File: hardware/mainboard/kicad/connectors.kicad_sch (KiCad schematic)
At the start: 14 parts, among them J5 GCT USB4105-GF-A-120, J6 4-pin pogo dock, J7 Tag-Connect TC2030-IDC-NL, U8 USBLC6-2SC6

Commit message: R30: align J6 bare contact BOM and J7 service header value with schematic
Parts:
- J6: now left out of the parts list
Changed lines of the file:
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@@
 	(global_label "USB_SHIELD" (shape input) (at 60.96 144.78 0) (effects (font (size 0.9 0.9)) (justify right bottom)))
 	(global_label "GND" (shape output) (at 76.2 144.78 180) (effects (font (size 0.9 0.9)) (justify right bottom)))
-	(symbol (lib_id "ENKU:DOCK4") (at 160.02 68.58 0) (unit 1) (exclude_from_sim no) (in_bom yes) (on_board yes) (dnp no)
+	(symbol (lib_id "ENKU:DOCK4") (at 160.02 68.58 0) (unit 1) (exclude_from_sim no) (in_bom no) (on_board yes) (dnp no)
 		(property "Reference" "J6" (at 150.02 52.58 0) (effects (font (size 0.9 0.9))))
 		(property "Value" "4-pin pogo dock" (at 170.02 52.58 0) (effects (font (size 0.9 0.9))))

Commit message: R41: correct ST ESD lands and route USB CC/VBUS power; fix GND clearances
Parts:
- U8: footprint Package_TO_SOT_SMD:SOT-23-6 -> ENKU:USBLC6_2SC6_ST_SOT23_6L
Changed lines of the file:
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@@
 		(property "Reference" "U8" (at 96.41 58.93 0) (effects (font (size 0.9 0.9))))
 		(property "Value" "USBLC6-2SC6" (at 114.41 58.93 0) (effects (font (size 0.9 0.9))))
-		(property "Footprint" "Package_TO_SOT_SMD:SOT-23-6" (at 105.41 74.93 0) (effects (font (size 0.9 0.9)) (hide yes)))
+		(property "Footprint" "ENKU:USBLC6_2SC6_ST_SOT23_6L" (at 105.41 74.93 0) (effects (font (size 0.9 0.9)) (hide yes)))
 		(property "Datasheet" "~" (at 105.41 74.93 0) (effects (font (size 0.9 0.9)) (hide yes)))
 		(property "Description" "USBLC6-2SC6" (at 105.41 74.93 0) (effects (font (size 0.9 0.9)) (hide yes)))

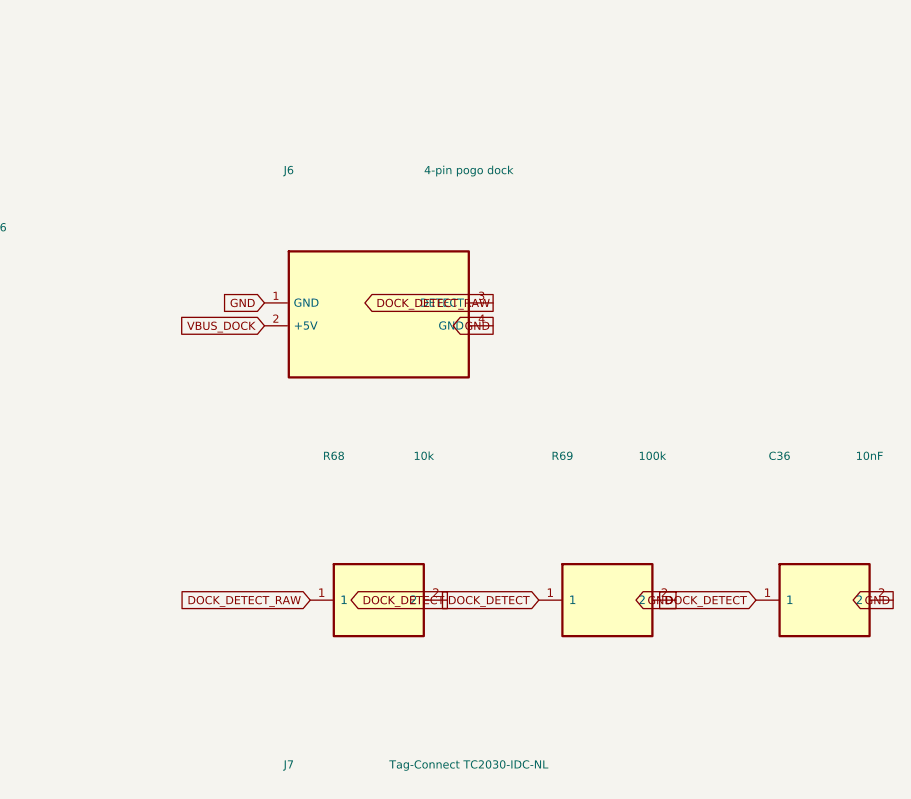
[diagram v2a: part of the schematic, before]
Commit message: hardware: preserve recovered R119 layout and verified R118 source [skip ci]
Persist the KiCad 10.0.7 project before the next routing pass. The recovered layout has 67 opens, ERC 0, parity 0 and zero RF keepout violations; routing is incomplete and fabrication is blocked. Preserve all pad and surviving copper net identities and retain an immutable R118 source archive.
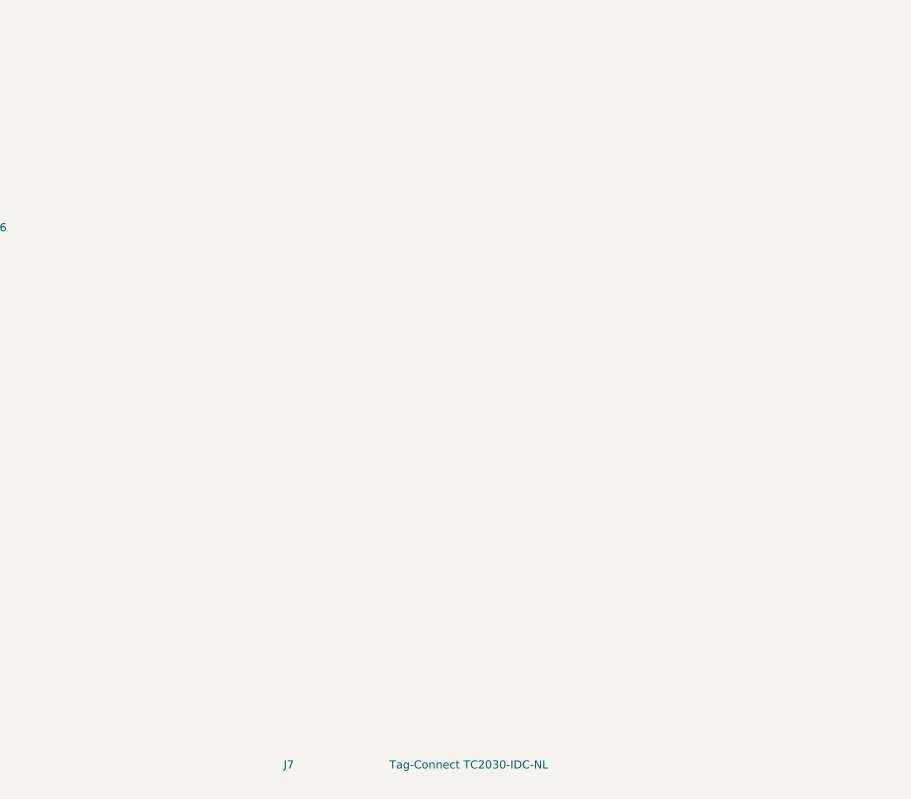
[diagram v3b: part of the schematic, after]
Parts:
- removed C36: 10nF, Capacitor_SMD:C_0603_1608Metric, symbol ENKU:C
- removed J6: 4-pin pogo dock, ENKU:DOCK_POGO_4, symbol ENKU:DOCK4
- removed R68: 10k, Resistor_SMD:R_0603_1608Metric, symbol ENKU:R
- removed R69: 100k, Resistor_SMD:R_0603_1608Metric, symbol ENKU:R
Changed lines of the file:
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@@
 	(global_label "USB_SHIELD" (shape input) (at 60.96 144.78 0) (effects (font (size 0.9 0.9)) (justify right bottom)))
 	(global_label "GND" (shape output) (at 76.2 144.78 180) (effects (font (size 0.9 0.9)) (justify right bottom)))
-	(symbol (lib_id "ENKU:DOCK4") (at 160.02 68.58 0) (unit 1) (exclude_from_sim no) (in_bom no) (on_board yes) (dnp no)
-		(property "Reference" "J6" (at 150.02 52.58 0) (effects (font (size 0.9 0.9))))
-		(property "Value" "4-pin pogo dock" (at 170.02 52.58 0) (effects (font (size 0.9 0.9))))
-		(property "Footprint" "ENKU:DOCK_POGO_4" (at 160.02 68.58 0) (effects (font (size 0.9 0.9)) (hide yes)))
-		(property "Datasheet" "~" (at 160.02 68.58 0) (effects (font (size 0.9 0.9)) (hide yes)))
-		(property "Description" "4-pin pogo dock" (at 160.02 68.58 0) (effects (font (size 0.9 0.9)) (hide yes)))
-		(pin "1")
-		(pin "2")
-		(pin "3")
-		(pin "4")
-		(instances (project "enku-mainboard-r0.1" (path "/10000000-0000-4000-8000-000000000001/73000000-0000-4000-8000-000000000084" (reference "J6") (unit 1))))
-	)
-	(global_label "GND" (shape input) (at 147.32 67.31 0) (effects (font (size 0.9 0.9)) (justify right bottom)))
-	(global_label "VBUS_DOCK" (shape input) (at 147.32 69.85 0) (effects (font (size 0.9 0.9)) (justify right bottom)))
-	(global_label "DOCK_DETECT_RAW" (shape output) (at 172.72 67.31 180) (effects (font (size 0.9 0.9)) (justify right bottom)))
-	(global_label "GND" (shape output) (at 172.72 69.85 180) (effects (font (size 0.9 0.9)) (justify right bottom)))
-	(symbol (lib_id "ENKU:R") (at 160.02 100.33 0) (unit 1) (exclude_from_sim no) (in_bom yes) (on_board yes) (dnp no)
-		(property "Reference" "R68" (at 155.02 84.33 0) (effects (font (size 0.9 0.9))))
-		(property "Value" "10k" (at 165.02 84.33 0) (effects (font (size 0.9 0.9))))
-		(property "Footprint" "Resistor_SMD:R_0603_1608Metric" (at 160.02 100.33 0) (effects (font (size 0.9 0.9)) (hide yes)))
-		(property "Datasheet" "~" (at 160.02 100.33 0) (effects (font (size 0.9 0.9)) (hide yes)))
-		(property "Description" "10k" (at 160.02 100.33 0) (effects (font (size 0.9 0.9)) (hide yes)))
-		(pin "1")
-		(pin "2")
-		(instances (project "enku-mainboard-r0.1" (path "/10000000-0000-4000-8000-000000000001/73000000-0000-4000-8000-000000000093" (reference "R68") (unit 1))))
-	)
-	(global_label "DOCK_DETECT_RAW" (shape input) (at 152.4 100.33 0) (effects (font (size 0.9 0.9)) (justify right bottom)))
-	(global_label "DOCK_DETECT" (shape output) (at 167.64 100.33 180) (effects (font (size 0.9 0.9)) (justify right bottom)))
-	(symbol (lib_id "ENKU:R") (at 185.42 100.33 0) (unit 1) (exclude_from_sim no) (in_bom yes) (on_board yes) (dnp no)
-		(property "Reference" "R69" (at 180.42 84.33 0) (effects (font (size 0.9 0.9))))
-		(property "Value" "100k" (at 190.42 84.33 0) (effects (font (size 0.9 0.9))))
-		(property "Footprint" "Resistor_SMD:R_0603_1608Metric" (at 185.42 100.33 0) (effects (font (size 0.9 0.9)) (hide yes)))
-		(property "Datasheet" "~" (at 185.42 100.33 0) (effects (font (size 0.9 0.9)) (hide yes)))
-		(property "Description" "100k" (at 185.42 100.33 0) (effects (font (size 0.9 0.9)) (hide yes)))
-		(pin "1")
-		(pin "2")
-		(instances (project "enku-mainboard-r0.1" (path "/10000000-0000-4000-8000-000000000001/73000000-0000-4000-8000-000000000098" (reference "R69") (unit 1))))
-	)
-	(global_label "DOCK_DETECT" (shape input) (at 177.8 100.33 0) (effects (font (size 0.9 0.9)) (justify right bottom)))
-	(global_label "GND" (shape output) (at 193.04 100.33 180) (effects (font (size 0.9 0.9)) (justify right bottom)))
-	(symbol (lib_id "ENKU:C") (at 209.55 100.33 0) (unit 1) (exclude_from_sim no) (in_bom yes) (on_board yes) (dnp no)
-		(property "Reference" "C36" (at 204.55 84.33 0) (effects (font (size 0.9 0.9))))
-		(property "Value" "10nF" (at 214.55 84.33 0) (effects (font (size 0.9 0.9))))
-		(property "Footprint" "Capacitor_SMD:C_0603_1608Metric" (at 209.55 100.33 0) (effects (font (size 0.9 0.9)) (hide yes)))
-		(property "Datasheet" "~" (at 209.55 100.33 0) (effects (font (size 0.9 0.9)) (hide yes)))
-		(property "Description" "10nF" (at 209.55 100.33 0) (effects (font (size 0.9 0.9)) (hide yes)))
-		(pin "1")
-		(pin "2")
-		(instances (project "enku-mainboard-r0.1" (path "/10000000-0000-4000-8000-000000000001/73000000-0000-4000-8000-000000000103" (reference "C36") (unit 1))))
-	)
-	(global_label "DOCK_DETECT" (shape input) (at 201.93 100.33 0) (effects (font (size 0.9 0.9)) (justify right bottom)))
-	(global_label "GND" (shape output) (at 217.17 100.33 180) (effects (font (size 0.9 0.9)) (justify right bottom)))
 	(symbol (lib_id "ENKU:DEBUG6") (at 160.02 134.62 0) (unit 1) (exclude_from_sim no) (in_bom no) (on_board yes) (dnp no)
 		(property "Reference" "J7" (at 150.02 118.62 0) (effects (font (size 0.9 0.9))))

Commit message: R126: select 61 exact components, correct physical lands and local routing, preserve full source; NO FAB
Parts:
- C35: footprint Capacitor_SMD:C_0603_1608Metric -> ENKU:C_CC0603_YAGEO_REFLOW_TRANSFER; Assembly (none) -> FIT; MPN (none) -> CC0603KRX7R9BB472; Manufacturer (none) -> Yageo; Voltage (none) -> 50V
- R62, R63: footprint Resistor_SMD:R_0603_1608Metric -> ENKU:R_RC0603_YAGEO_REFLOW; Assembly (none) -> FIT; MPN (none) -> RC0603FR-075K1L; Manufacturer (none) -> Yageo
- R64, R65: footprint Resistor_SMD:R_0603_1608Metric -> ENKU:R_RC0603_YAGEO_REFLOW; Assembly (none) -> FIT; MPN (none) -> RC0603JR-070RL; Manufacturer (none) -> Yageo; Tuning MPN (none) -> RC0603FR-0722RL
- R66: footprint Resistor_SMD:R_0603_1608Metric -> ENKU:R_RC0603_YAGEO_REFLOW; Assembly (none) -> FIT; MPN (none) -> RC0603FR-071ML; Manufacturer (none) -> Yageo
- R67: footprint Resistor_SMD:R_0603_1608Metric -> ENKU:R_RC0603_YAGEO_REFLOW; Assembly (none) -> DNP; MPN (none) -> RC0603JR-070RL; Manufacturer (none) -> Yageo
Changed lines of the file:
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@@
 		(property "Reference" "R62" (at 22.94 103.38 0) (effects (font (size 0.9 0.9))))
 		(property "Value" "5.1k 1%" (at 32.94 103.38 0) (effects (font (size 0.9 0.9))))
-		(property "Footprint" "Resistor_SMD:R_0603_1608Metric" (at 27.94 119.38 0) (effects (font (size 0.9 0.9)) (hide yes)))
-		(property "Datasheet" "~" (at 27.94 119.38 0) (effects (font (size 0.9 0.9)) (hide yes)))
+		(property "Footprint" "ENKU:R_RC0603_YAGEO_REFLOW" (at 27.94 119.38 0) (effects (font (size 0.9 0.9)) (hide yes)))
+		(property "Datasheet" "https://yageogroup.com/content/datasheet/asset/file/PYU-RC_GROUP_51_ROHS_L" (at 27.94 119.38 0) (effects (font (size 0.9 0.9)) (hide yes)))
 		(property "Description" "5.1k 1%" (at 27.94 119.38 0) (effects (font (size 0.9 0.9)) (hide yes)))
 		(pin "1")
 		(pin "2")
 		(instances (project "enku-mainboard-r0.1" (path "/10000000-0000-4000-8000-000000000001/73000000-0000-4000-8000-000000000036" (reference "R62") (unit 1))))
+		(property "MPN" "RC0603FR-075K1L" (at 0 0 0) (effects (font (size .8 .8)) (hide yes)))
+		(property "Manufacturer" "Yageo" (at 0 0 0) (effects (font (size .8 .8)) (hide yes)))
+		(property "Assembly" "FIT" (at 0 0 0) (effects (font (size .8 .8)) (hide yes)))
 	)
 	(global_label "USB_CC1" (shape input) (at 20.32 119.38 0) (effects (font (size 0.9 0.9)) (justify right bottom)))
@@
 		(property "Reference" "R63" (at 43.26 103.38 0) (effects (font (size 0.9 0.9))))
 		(property "Value" "5.1k 1%" (at 53.26 103.38 0) (effects (font (size 0.9 0.9))))
-		(property "Footprint" "Resistor_SMD:R_0603_1608Metric" (at 48.26 119.38 0) (effects (font (size 0.9 0.9)) (hide yes)))
-		(property "Datasheet" "~" (at 48.26 119.38 0) (effects (font (size 0.9 0.9)) (hide yes)))
+		(property "Footprint" "ENKU:R_RC0603_YAGEO_REFLOW" (at 48.26 119.38 0) (effects (font (size 0.9 0.9)) (hide yes)))
+		(property "Datasheet" "https://yageogroup.com/content/datasheet/asset/file/PYU-RC_GROUP_51_ROHS_L" (at 48.26 119.38 0) (effects (font (size 0.9 0.9)) (hide yes)))
 		(property "Description" "5.1k 1%" (at 48.26 119.38 0) (effects (font (size 0.9 0.9)) (hide yes)))
 		(pin "1")
 		(pin "2")
 		(instances (project "enku-mainboard-r0.1" (path "/10000000-0000-4000-8000-000000000001/73000000-0000-4000-8000-000000000041" (reference "R63") (unit 1))))
+		(property "MPN" "RC0603FR-075K1L" (at 0 0 0) (effects (font (size .8 .8)) (hide yes)))
+		(property "Manufacturer" "Yageo" (at 0 0 0) (effects (font (size .8 .8)) (hide yes)))
+		(property "Assembly" "FIT" (at 0 0 0) (effects (font (size .8 .8)) (hide yes)))
 	)
 	(global_label "USB_CC2" (shape input) (at 40.64 119.38 0) (effects (font (size 0.9 0.9)) (justify right bottom)))
@@
 		(property "Reference" "R64" (at 80.09 103.38 0) (effects (font (size 0.9 0.9))))
 		(property "Value" "0R (22R tune)" (at 90.09 103.38 0) (effects (font (size 0.9 0.9))))
-		(property "Footprint" "Resistor_SMD:R_0603_1608Metric" (at 85.09 119.38 0) (effects (font (size 0.9 0.9)) (hide yes)))
-		(property "Datasheet" "~" (at 85.09 119.38 0) (effects (font (size 0.9 0.9)) (hide yes)))
+		(property "Footprint" "ENKU:R_RC0603_YAGEO_REFLOW" (at 85.09 119.38 0) (effects (font (size 0.9 0.9)) (hide yes)))
+		(property "Datasheet" "https://yageogroup.com/content/datasheet/asset/file/PYU-RC_GROUP_51_ROHS_L" (at 85.09 119.38 0) (effects (font (size 0.9 0.9)) (hide yes)))
 		(property "Description" "0R (22R tune)" (at 85.09 119.38 0) (effects (font (size 0.9 0.9)) (hide yes)))
 		(pin "1")
 		(pin "2")
 		(instances (project "enku-mainboard-r0.1" (path "/10000000-0000-4000-8000-000000000001/73000000-0000-4000-8000-000000000046" (reference "R64") (unit 1))))
+		(property "MPN" "RC0603JR-070RL" (at 0 0 0) (effects (font (size .8 .8)) (hide yes)))
+		(property "Manufacturer" "Yageo" (at 0 0 0) (effects (font (size .8 .8)) (hide yes)))
+		(property "Assembly" "FIT" (at 0 0 0) (effects (font (size .8 .8)) (hide yes)))
+		(property "Tuning MPN" "RC0603FR-0722RL" (at 0 0 0) (effects (font (size .8 .8)) (hide yes)))
 	)
 	(global_label "USB_DP_CONN" (shape input) (at 77.47 119.38 0) (effects (font (size 0.9 0.9)) (justify right bottom)))
@@
 		(property "Reference" "R65" (at 100.41 103.38 0) (effects (font (size 0.9 0.9))))
 		(property "Value" "0R (22R tune)" (at 110.41 103.38 0) (effects (font (size 0.9 0.9))))
-		(property "Footprint" "Resistor_SMD:R_0603_1608Metric" (at 105.41 119.38 0) (effects (font (size 0.9 0.9)) (hide yes)))
-		(property "Datasheet" "~" (at 105.41 119.38 0) (effects (font (size 0.9 0.9)) (hide yes)))
+		(property "Footprint" "ENKU:R_RC0603_YAGEO_REFLOW" (at 105.41 119.38 0) (effects (font (size 0.9 0.9)) (hide yes)))
+		(property "Datasheet" "https://yageogroup.com/content/datasheet/asset/file/PYU-RC_GROUP_51_ROHS_L" (at 105.41 119.38 0) (effects (font (size 0.9 0.9)) (hide yes)))
 		(property "Description" "0R (22R tune)" (at 105.41 119.38 0) (effects (font (size 0.9 0.9)) (hide yes)))
 		(pin "1")
 		(pin "2")
 		(instances (project "enku-mainboard-r0.1" (path "/10000000-0000-4000-8000-000000000001/73000000-0000-4000-8000-000000000051" (reference "R65") (unit 1))))
+		(property "MPN" "RC0603JR-070RL" (at 0 0 0) (effects (font (size .8 .8)) (hide yes)))
+		(property "Manufacturer" "Yageo" (at 0 0 0) (effects (font (size .8 .8)) (hide yes)))
+		(property "Assembly" "FIT" (at 0 0 0) (effects (font (size .8 .8)) (hide yes)))
+		(property "Tuning MPN" "RC0603FR-0722RL" (at 0 0 0) (effects (font (size .8 .8)) (hide yes)))
 	)
 	(global_label "USB_DM_CONN" (shape input) (at 97.79 119.38 0) (effects (font (size 0.9 0.9)) (justify right bottom)))
@@
 		(property "Reference" "R66" (at 22.94 128.78 0) (effects (font (size 0.9 0.9))))
 		(property "Value" "1M" (at 32.94 128.78 0) (effects (font (size 0.9 0.9))))
-		(property "Footprint" "Resistor_SMD:R_0603_1608Metric" (at 27.94 144.78 0) (effects (font (size 0.9 0.9)) (hide yes)))
-		(property "Datasheet" "~" (at 27.94 144.78 0) (effects (font (size 0.9 0.9)) (hide yes)))
+		(property "Footprint" "ENKU:R_RC0603_YAGEO_REFLOW" (at 27.94 144.78 0) (effects (font (size 0.9 0.9)) (hide yes)))
+		(property "Datasheet" "https://yageogroup.com/content/datasheet/asset/file/PYU-RC_GROUP_51_ROHS_L" (at 27.94 144.78 0) (effects (font (size 0.9 0.9)) (hide yes)))
 		(property "Description" "1M" (at 27.94 144.78 0) (effects (font (size 0.9 0.9)) (hide yes)))
 		(pin "1")
 		(pin "2")
 		(instances (project "enku-mainboard-r0.1" (path "/10000000-0000-4000-8000-000000000001/73000000-0000-4000-8000-000000000069" (reference "R66") (unit 1))))
+		(property "MPN" "RC0603FR-071ML" (at 0 0 0) (effects (font (size .8 .8)) (hide yes)))
+		(property "Manufacturer" "Yageo" (at 0 0 0) (effects (font (size .8 .8)) (hide yes)))
+		(property "Assembly" "FIT" (at 0 0 0) (effects (font (size .8 .8)) (hide yes)))
 	)
 	(global_label "USB_SHIELD" (shape input) (at 20.32 144.78 0) (effects (font (size 0.9 0.9)) (justify right bottom)))
@@
 		(property "Reference" "C35" (at 43.26 128.78 0) (effects (font (size 0.9 0.9))))
 		(property "Value" "4.7nF" (at 53.26 128.78 0) (effects (font (size 0.9 0.9))))
-		(property "Footprint" "Capacitor_SMD:C_0603_1608Metric" (at 48.26 144.78 0) (effects (font (size 0.9 0.9)) (hide yes)))
-		(property "Datasheet" "~" (at 48.26 144.78 0) (effects (font (size 0.9 0.9)) (hide yes)))
+		(property "Footprint" "ENKU:C_CC0603_YAGEO_REFLOW_TRANSFER" (at 48.26 144.78 0) (effects (font (size 0.9 0.9)) (hide yes)))
+		(property "Datasheet" "https://yageogroup.com/download/specsheet/CC0603KRX7R9BB472" (at 48.26 144.78 0) (effects (font (size 0.9 0.9)) (hide yes)))
 		(property "Description" "4.7nF" (at 48.26 144.78 0) (effects (font (size 0.9 0.9)) (hide yes)))
 		(pin "1")
 		(pin "2")
 		(instances (project "enku-mainboard-r0.1" (path "/10000000-0000-4000-8000-000000000001/73000000-0000-4000-8000-000000000074" (reference "C35") (unit 1))))
+		(property "MPN" "CC0603KRX7R9BB472" (at 0 0 0) (effects (font (size .8 .8)) (hide yes)))
+		(property "Manufacturer" "Yageo" (at 0 0 0) (effects (font (size .8 .8)) (hide yes)))
+		(property "Assembly" "FIT" (at 0 0 0) (effects (font (size .8 .8)) (hide yes)))
+		(property "Voltage" "50V" (at 0 0 0) (effects (font (size .8 .8)) (hide yes)))
 	)
 	(global_label "USB_SHIELD" (shape input) (at 40.64 144.78 0) (effects (font (size 0.9 0.9)) (justify right bottom)))
@@
 		(property "Reference" "R67" (at 63.58 128.78 0) (effects (font (size 0.9 0.9))))
 		(property "Value" "0R DNP" (at 73.58 128.78 0) (effects (font (size 0.9 0.9))))
-		(property "Footprint" "Resistor_SMD:R_0603_1608Metric" (at 68.58 144.78 0) (effects (font (size 0.9 0.9)) (hide yes)))
-		(property "Datasheet" "~" (at 68.58 144.78 0) (effects (font (size 0.9 0.9)) (hide yes)))
+		(property "Footprint" "ENKU:R_RC0603_YAGEO_REFLOW" (at 68.58 144.78 0) (effects (font (size 0.9 0.9)) (hide yes)))
+		(property "Datasheet" "https://yageogroup.com/content/datasheet/asset/file/PYU-RC_GROUP_51_ROHS_L" (at 68.58 144.78 0) (effects (font (size 0.9 0.9)) (hide yes)))
 		(property "Description" "0R DNP" (at 68.58 144.78 0) (effects (font (size 0.9 0.9)) (hide yes)))
 		(pin "1")
 		(pin "2")
 		(instances (project "enku-mainboard-r0.1" (path "/10000000-0000-4000-8000-000000000001/73000000-0000-4000-8000-000000000079" (reference "R67") (unit 1))))
+		(property "MPN" "RC0603JR-070RL" (at 0 0 0) (effects (font (size .8 .8)) (hide yes)))
+		(property "Manufacturer" "Yageo" (at 0 0 0) (effects (font (size .8 .8)) (hide yes)))
+		(property "Assembly" "DNP" (at 0 0 0) (effects (font (size .8 .8)) (hide yes)))
 	)
 	(global_label "USB_SHIELD" (shape input) (at 60.96 144.78 0) (effects (font (size 0.9 0.9)) (justify right bottom)))
